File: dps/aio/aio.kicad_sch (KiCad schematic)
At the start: 9 parts, among them U24 AIO_outline, U25 INA186A3IDCKR

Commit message: feat: draw the clear part of the H743 core, document the AIO, and explain it on an interactive page
- mcu_h743: STM32H743VIH6 (TFBGA-100) with supply and decoupling per ST
  AN4938 (100 nF per VDD + 4.7 uF, VDDLDO 4.7 uF, VCAP1+VCAP2 joined with
  2x 2.2 uF, VDDA and VDD33USB 100 nF + 1 uF, VBAT 100 nF), BOOT0 and
  PDR_ON, SWD/DFU pads, USB-C from OpenAIO, battery divider 100k/10k and
  I2C2 pull-ups; every pin labelled per the MicoAir743v2 hwdef. Crystal,
  baro, logging, second IMU and peripheral connectors stay open.
- IMU INT2 (OpenAIO's CLKIN) left unconnected, as on the MicoAir; +5V_USB
  joins the power sheet; ERC is down to 17 errors, all explained.
- NAVRH.md: every sheet and block with its source and reason, the power
  tree, connectors, ArduPilot settings and open questions; tabulky.py
  regenerates its pin map, cross-sheet nets and BOM from the netlist.
- web/: build.py turns the schematic into one page with clickable blocks
  (what, why, where from), texts in obsah.py; the 5 MB output is ignored.

Co-Authored-By: Claude Opus 5.5 <noreply@anthropic.com>
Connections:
- no-connect marks 0 -> 1
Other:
- sheet MCU H743 ports: added none; removed IMU_CLKIN
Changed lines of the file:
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@@
 		)
 	)
-	(wire
-		(pts
-			(xy 167.64 213.36)
-			(xy 170.18 213.36)
-		)
-		(stroke
-			(width 0)
-			(type default)
-		)
-	)
-	(label "IMU_CLKIN"
-		(at 170.18 213.36 0)
-		(effects
-			(font
-				(size 1.27 1.27)
-			)
-			(justify left bottom)
-		)
+	(no_connect
+		(at 167.64 213.36)
 	)
 	(wire
@@
 			)
 		)
-		(pin "IMU_CLKIN" bidirectional
+		(pin "ESC_CURRENT" bidirectional
 			(at 132.08 114.3 180)
 			(effects
@@
 			)
 		)
-		(pin "ESC_CURRENT" bidirectional
+		(pin "SDA" bidirectional
 			(at 132.08 116.84 180)
 			(effects
@@
 			)
 		)
-		(pin "SDA" bidirectional
+		(pin "SCL" bidirectional
 			(at 132.08 119.38 180)
-			(effects
-				(font
-					(size 1.27 1.27)
-				)
-				(justify left)
-			)
-		)
-		(pin "SCL" bidirectional
-			(at 132.08 121.92 180)
 			(effects
 				(font
@@
 		)
 	)
-	(label "IMU_CLKIN"
+	(label "ESC_CURRENT"
 		(at 129.54 114.3 180)
 		(effects
@@
 		)
 	)
-	(label "ESC_CURRENT"
+	(label "SDA"
 		(at 129.54 116.84 180)
 		(effects
@@
 		)
 	)
-	(label "SDA"
+	(label "SCL"
 		(at 129.54 119.38 180)
 		(effects
 			(font
-				(size 1.27 1.27)
-			)
-			(justify right bottom)
-		)
-	)
-	(wire
-		(pts
-			(xy 132.08 121.92)
-			(xy 129.54 121.92)
-		)
-		(stroke
-			(width 0)
-			(type default)
-		)
-	)
-	(label "SCL"
-		(at 129.54 121.92 180)
-		(effects
-			(font

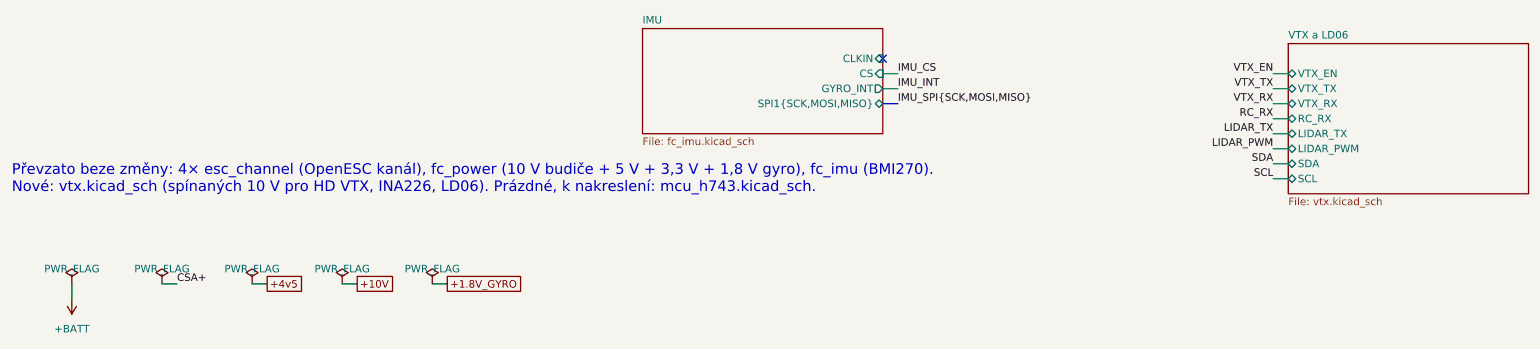
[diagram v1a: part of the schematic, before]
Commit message: feat: draw the AIO's RGB LED and buzzer switch, and keep the schematic generator in the repo
- D301-D303 XINGLIGHT XL-1005 0402 with anodes on 3.3 V: ArduPilot's
  GPIO_LED_RGB lights with a low (HAL_GPIO_LED_ON 0). Green and blue are
  OpenAIO's parts, red C965790 from the same series; 330R/150R/75R, ~3-5 mA.
- Q301 AO3400A low-side switch for an external active 5 V buzzer on pads
  BZ+/BZ- (BUZZ_ON_LVL 1), R319 holds it off through reset, D304 1N4148WS
  across the buzzer. A 2N7002 (Vgs(th) up to 2.5 V) would barely open at 3.3 V.
- dps/aio/gen/gen_aio.py writes every sheet with stable UUIDs; it now finds
  OpenAIO and KiCad's symbols on its own and only copies the board, rules,
  project and footprints when they are missing.
- NAVRH, README, web texts and tables follow; ERC still 18, explained.

Co-Authored-By: Claude Opus 5.5 <noreply@anthropic.com>
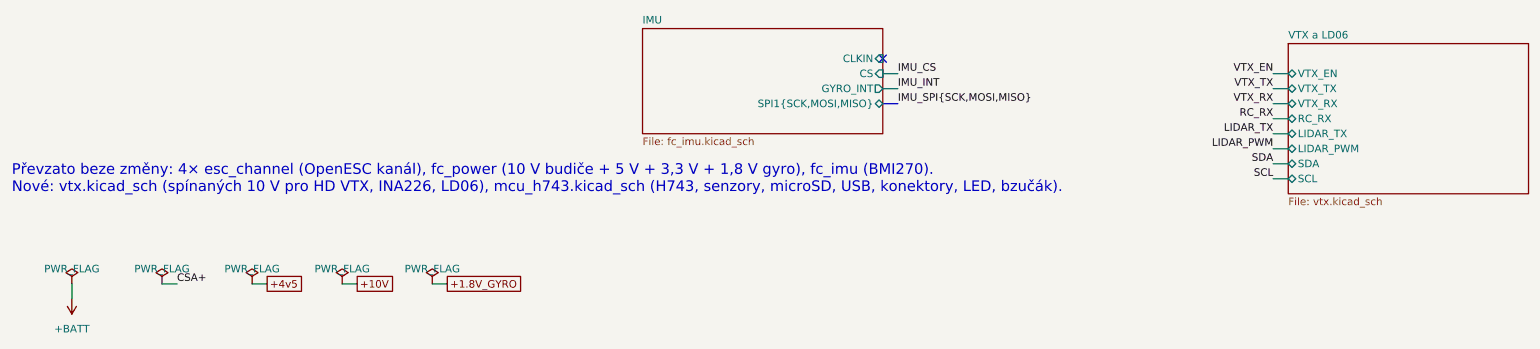
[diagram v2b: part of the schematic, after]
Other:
- note added: "Převzato beze změny: 4× esc_channel (OpenESC kanál), fc_power (10 V budiče + 5 V + 3,3 V + 1,8 V gyro), fc_imu (BMI270). Nové: vtx.kicad_sch (spínaných 10 V pro HD VTX, INA226, LD06), mcu_h743.kicad_sch (H743, senzory, microSD, USB, konektory, LED, bzučák)."
- note removed: "Převzato beze změny: 4× esc_channel (OpenESC kanál), fc_power (10 V budiče + 5 V + 3,3 V + 1,8 V gyro), fc_imu (BMI270). Nové: vtx.kicad_sch (spínaných 10 V pro HD VTX, INA226, LD06). Prázdné, k nakreslení: mcu_h743.kicad_sch."
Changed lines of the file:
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@@
 		)
 	)
-	(text "Převzato beze změny: 4× esc_channel (OpenESC kanál), fc_power (10 V budiče + 5 V + 3,3 V + 1,8 V gyro), fc_imu (BMI270).\nNové: vtx.kicad_sch (spínaných 10 V pro HD VTX, INA226, LD06). Prázdné, k nakreslení: mcu_h743.kicad_sch."
+	(text "Převzato beze změny: 4× esc_channel (OpenESC kanál), fc_power (10 V budiče + 5 V + 3,3 V + 1,8 V gyro), fc_imu (BMI270).\nNové: vtx.kicad_sch (spínaných 10 V pro HD VTX, INA226, LD06), mcu_h743.kicad_sch (H743, senzory, microSD, USB, konektory, LED, bzučák)."
 		(exclude_from_sim no)
 		(at 20.32 236.22 0)

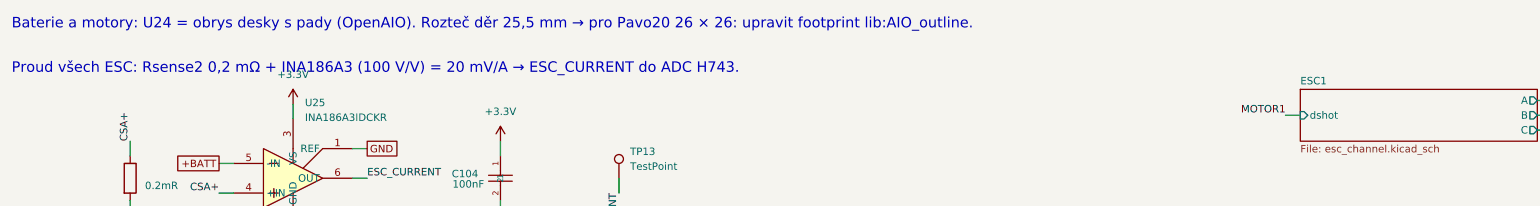
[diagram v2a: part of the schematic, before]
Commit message: docs: keep the AIO's OpenAIO outline and 25.5 mm holes
Slotting the holes to 25.5-26 mm puts the top-left slot into 8 of the
~40 /CSA+ vias that carry battery current around it (DRC tried on the
board, then reverted). An M2 screw on the Pavo20's 26 mm pitch still
passes a 3 mm hole on 25.5 with 0.15 mm to spare, as on MicoAir, and the
35.4 mm outline is smaller than the 36 mm we had copied from MicoAir.

Co-Authored-By: Claude Opus 5.5 <noreply@anthropic.com>
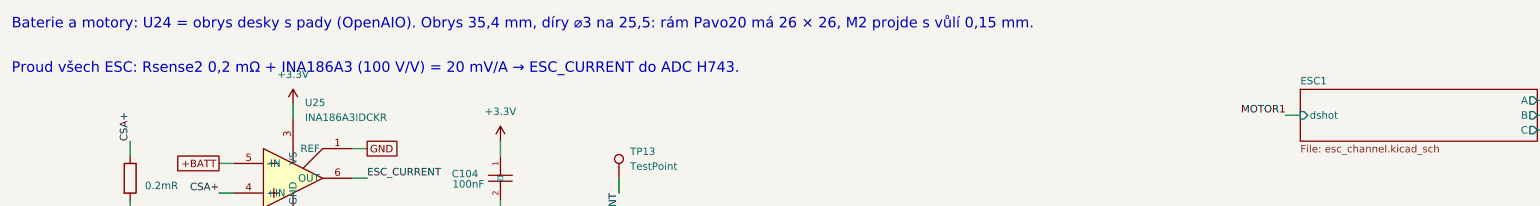
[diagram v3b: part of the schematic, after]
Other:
- note added: "Baterie a motory: U24 = obrys desky s pady (OpenAIO). Obrys 35,4 mm, díry ⌀3 na 25,5: rám Pavo20 má 26 × 26, M2 projde s vůlí 0,15 mm."
- note removed: "Baterie a motory: U24 = obrys desky s pady (OpenAIO). Rozteč děr 25,5 mm → pro Pavo20 26 × 26: upravit footprint lib:AIO_outline."
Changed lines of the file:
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@@
 		)
 	)
-	(text "Baterie a motory: U24 = obrys desky s pady (OpenAIO). Rozteč děr 25,5 mm → pro Pavo20 26 × 26: upravit footprint lib:AIO_outline."
+	(text "Baterie a motory: U24 = obrys desky s pady (OpenAIO). Obrys 35,4 mm, díry ⌀3 na 25,5: rám Pavo20 má 26 × 26, M2 projde s vůlí 0,15 mm."
 		(exclude_from_sim no)
 		(at 20.32 25.4 0)

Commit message: feat: put all four MicoAir connectors on the AIO's edge and place it without the INA226
- The edge search found four spots no kept OpenAIO part blocks, so the ESCs
  stay as they are: J201 VTX front bottom, J303 GPS front right below motor 4,
  J305 UART1+UART6 back right, J304 UART4 back bottom. Motor pads are front
  only and the battery pads take the top edge, hence not MicoAir's places.
- Pads as on MicoAir: new lib:Pad_1.0x1.4mm (courtyard 1.2 x 1.6) instead of
  1 mm round test points with a 2 x 2 courtyard.
- Dropped for room, none of them on MicoAir: the VTX INA226 with its shunt,
  JP201 and the buzzer diode; Q301 is OpenAIO's AP1606 in DFN 1.0 x 0.6
  instead of an AO3400A in SOT-23. BATT2 defaults go; firmware rebuilt.
- Placement now treats pads, holes on both sides and the outer-layer copper
  of nets no new part uses (ESC inside, +BATT, the CSA+ via field) as
  obstacles, in 1 mm cells. vycisti_med.py removes the dangling RP2354
  leftovers and copper the new parts land on, never CSA+ or +BATT; the
  updater swaps changed footprints and sets sheet names.
- U303 (BMI088) and U201 (VTX buck) do not fit: no 3.3 x 3.3 mm is left on
  either side. DRC: 163 unconnected, otherwise OpenAIO's own warnings.

Co-Authored-By: Claude Opus 5.5 <noreply@anthropic.com>
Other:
- sheet MCU H743 ports: added none; removed SCL, SDA
- sheet VTX a LD06 ports: added none; removed SCL, SDA
- note added: "Převzato beze změny: 4× esc_channel (OpenESC kanál), fc_power (10 V budiče + 5 V + 3,3 V + 1,8 V gyro), fc_imu (BMI270). Nové: vtx.kicad_sch (spínaných 10 V pro HD VTX, LD06), mcu_h743.kicad_sch (H743, senzory, microSD, USB, konektory, LED, bzučák)."
- note removed: "Převzato beze změny: 4× esc_channel (OpenESC kanál), fc_power (10 V budiče + 5 V + 3,3 V + 1,8 V gyro), fc_imu (BMI270). Nové: vtx.kicad_sch (spínaných 10 V pro HD VTX, INA226, LD06), mcu_h743.kicad_sch (H743, senzory, microSD, USB, konektory, LED, bzučák)."
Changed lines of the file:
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@@
 	(sheet
 		(at 236.22 210.82)
-		(size 40.64 25.4)
+		(size 40.64 20.32)
 		(exclude_from_sim no)
 		(in_bom yes)
@@
 		)
 		(property "Sheetfile" "vtx.kicad_sch"
-			(at 236.22 236.8084 0)
+			(at 236.22 231.7284 0)
 			(effects
 				(font
@@
 		(pin "LIDAR_PWM" bidirectional
 			(at 236.22 228.6 180)
-			(effects
-				(font
-					(size 1.27 1.27)
-				)
-				(justify left)
-			)
-		)
-		(pin "SDA" bidirectional
-			(at 236.22 231.14 180)
-			(effects
-				(font
-					(size 1.27 1.27)
-				)
-				(justify left)
-			)
-		)
-		(pin "SCL" bidirectional
-			(at 236.22 233.68 180)
 			(effects
 				(font
@@
 	(label "LIDAR_PWM"
 		(at 233.68 228.6 180)
-		(effects
-			(font
-				(size 1.27 1.27)
-			)
-			(justify right bottom)
-		)
-	)
-	(wire
-		(pts
-			(xy 236.22 231.14)
-			(xy 233.68 231.14)
-		)
-		(stroke
-			(width 0)
-			(type default)
-		)
-	)
-	(label "SDA"
-		(at 233.68 231.14 180)
-		(effects
-			(font
-				(size 1.27 1.27)
-			)
-			(justify right bottom)
-		)
-	)
-	(wire
-		(pts
-			(xy 236.22 233.68)
-			(xy 233.68 233.68)
-		)
-		(stroke
-			(width 0)
-			(type default)
-		)
-	)
-	(label "SCL"
-		(at 233.68 233.68 180)
 		(effects
 			(font
@@
 			)
 		)
-		(pin "SDA" bidirectional
-			(at 132.08 116.84 180)
-			(effects
-				(font
-					(size 1.27 1.27)
-				)
-				(justify left)
-			)
-		)
-		(pin "SCL" bidirectional
-			(at 132.08 119.38 180)
-			(effects
-				(font
-					(size 1.27 1.27)
-				)
-				(justify left)
-			)
-		)
 		(pin "MOTOR1" bidirectional
 			(at 182.88 106.68 0)
@@
 	(label "ESC_CURRENT"
 		(at 129.54 114.3 180)
-		(effects
-			(font
-				(size 1.27 1.27)
-			)
-			(justify right bottom)
-		)
-	)
-	(wire
-		(pts
-			(xy 132.08 116.84)
-			(xy 129.54 116.84)
-		)
-		(stroke
-			(width 0)
-			(type default)
-		)
-	)
-	(label "SDA"
-		(at 129.54 116.84 180)
-		(effects
-			(font
-				(size 1.27 1.27)
-			)
-			(justify right bottom)
-		)
-	)
-	(wire
-		(pts
-			(xy 132.08 119.38)
-			(xy 129.54 119.38)
-		)
-		(stroke
-			(width 0)
-			(type default)
-		)
-	)
-	(label "SCL"
-		(at 129.54 119.38 180)
 		(effects
 			(font
@@
 		)
 	)
-	(text "Převzato beze změny: 4× esc_channel (OpenESC kanál), fc_power (10 V budiče + 5 V + 3,3 V + 1,8 V gyro), fc_imu (BMI270).\nNové: vtx.kicad_sch (spínaných 10 V pro HD VTX, INA226, LD06), mcu_h743.kicad_sch (H743, senzory, microSD, USB, konektory, LED, bzučák)."
+	(text "Převzato beze změny: 4× esc_channel (OpenESC kanál), fc_power (10 V budiče + 5 V + 3,3 V + 1,8 V gyro), fc_imu (BMI270).\nNové: vtx.kicad_sch (spínaných 10 V pro HD VTX, LD06), mcu_h743.kicad_sch (H743, senzory, microSD, USB, konektory, LED, bzučák)."
 		(exclude_from_sim no)
 		(at 20.32 236.22 0)
